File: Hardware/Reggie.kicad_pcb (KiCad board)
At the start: 4 copper layers, 76 parts, among them J1 RBUS, J2 USB_C_Receptacle_USB2.0, U1 ESP32-S3, U2 SN65HVD230, U3 LM66200DRLR, U4 MAX77827AEFD+T, U5 SC4215ASTRT, Y1 R940000171

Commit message: 2nd review of schematic
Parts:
- added C25: 1uF, Capacitor_SMD:C_0402_1005Metric, F.Cu at (86.1, 24.0)
- added C26: 1uF, Capacitor_SMD:C_0402_1005Metric, F.Cu at (86.1, 26.0)
- added C27: 220nF, Capacitor_SMD:C_0402_1005Metric, F.Cu at (86.1, 27.9)
- added C28: 10nF, Capacitor_SMD:C_0402_1005Metric, F.Cu at (86.1, 29.9)
- added C29: 10nF, Capacitor_SMD:C_0402_1005Metric, F.Cu at (86.1, 31.9)
- added C30: 10nF, Capacitor_SMD:C_0402_1005Metric, F.Cu at (86.1, 33.9)
- added C31: 0.01uF, Capacitor_SMD:C_0402_1005Metric, F.Cu at (110.3, 59.0)
- added C32: 0.1uF, Capacitor_SMD:C_0402_1005Metric, F.Cu at (110.3, 61.0)
- added C33: 0.01uF, Capacitor_SMD:C_0402_1005Metric, F.Cu at (110.3, 63.0)
- added C34: 0.1uF, Capacitor_SMD:C_0402_1005Metric, F.Cu at (110.3, 64.9)
- added C35: 0.1uF, Capacitor_SMD:C_0402_1005Metric, F.Cu at (110.3, 66.9)
- added C36: 0.01uF, Capacitor_SMD:C_0402_1005Metric, F.Cu at (113.2, 59.0)
- added C37: 0.1uF, Capacitor_SMD:C_0402_1005Metric, F.Cu at (113.2, 61.0)
- added C38: 0.01uF, Capacitor_SMD:C_0402_1005Metric, F.Cu at (113.2, 63.0)
- added C39: 0.1uF, Capacitor_SMD:C_0402_1005Metric, F.Cu at (113.2, 64.9)
- added C40: 0.1uF, Capacitor_SMD:C_0402_1005Metric, F.Cu at (113.2, 66.9)
- added C41: 2.2uF, Capacitor_SMD:C_0603_1608Metric, F.Cu at (80.6, 58.0)
- added C42: 180pF, Capacitor_SMD:C_0402_1005Metric, F.Cu at (66.9, 63.0)
- added C43: 3.9nF, Capacitor_SMD:C_0402_1005Metric, F.Cu at (66.9, 65.0)
- added C44: 1uF, Capacitor_SMD:C_0402_1005Metric, F.Cu at (66.9, 66.9)
- added C45: 22uF, Capacitor_SMD:C_0805_2012Metric, F.Cu at (76.4, 58.3)
- added C46: 22uF, Capacitor_SMD:C_0805_2012Metric, F.Cu at (76.4, 61.3)
- added C47: 100nF, Capacitor_SMD:C_0402_1005Metric, F.Cu at (66.9, 68.9)
- added C48: 2.2uF, Capacitor_SMD:C_0402_1005Metric, F.Cu at (66.9, 70.9)
- added C49: 100nF, Capacitor_SMD:C_0402_1005Metric, F.Cu at (69.8, 63.0)
- added C50: 47uF, Capacitor_SMD:C_1206_3216Metric, F.Cu at (77.0, 51.7)
- added C51: 10uF, Capacitor_SMD:C_0603_1608Metric, F.Cu at (80.6, 60.5)
- added C52: 100nF, Capacitor_SMD:C_0402_1005Metric, F.Cu at (69.8, 65.0)
- added C53: 1uF, Capacitor_SMD:C_0402_1005Metric, F.Cu at (69.8, 66.9)
- added C54: 10uF, Capacitor_SMD:C_0603_1608Metric, F.Cu at (80.6, 63.0)
- added C55: 120pF, Capacitor_SMD:C_0402_1005Metric, F.Cu at (69.8, 68.9)
- added C56: 2.2nF, Capacitor_SMD:C_0402_1005Metric, F.Cu at (69.8, 70.9)
- added C57: 22uF, Capacitor_SMD:C_0805_2012Metric, F.Cu at (76.4, 64.3)
- added C58: 2.2uF, Capacitor_SMD:C_0402_1005Metric, F.Cu at (72.6, 63.0)
- added C59: 22uF, Capacitor_SMD:C_0805_2012Metric, F.Cu at (76.4, 67.3)
- added C60: 100nF, Capacitor_SMD:C_0402_1005Metric, F.Cu at (72.6, 65.0)
- added C61: 100nF, Capacitor_SMD:C_0402_1005Metric, F.Cu at (72.6, 66.9)
- added C62: 10uF, Capacitor_SMD:C_0603_1608Metric, F.Cu at (80.6, 65.5)
- added C63: 100nF, Capacitor_SMD:C_0402_1005Metric, F.Cu at (72.6, 68.9)
- added C64: 22uF, Capacitor_SMD:C_1206_3216Metric, F.Cu at (77.0, 55.1)
- added C65: 1uF, Capacitor_SMD:C_0402_1005Metric, F.Cu at (102.5, 31.1)
- added C66: 4.7uF, Capacitor_SMD:C_0402_1005Metric, F.Cu at (102.5, 33.1)
- added C67: 100uF, Capacitor_Tantalum_SMD:CP_EIA-7360-38_Kemet-E, F.Cu at (106.0, 12.9)
- added C68: 47uF, Capacitor_SMD:C_1206_3216Metric, F.Cu at (98.2, 10.8)
- added C69: 47uF, Capacitor_SMD:C_1206_3216Metric, F.Cu at (98.2, 14.1)
- added C70: 100nF, Capacitor_SMD:C_0402_1005Metric, F.Cu at (102.5, 35.1)
- added C71: 47uF, Capacitor_SMD:C_1206_3216Metric, F.Cu at (98.2, 17.5)
- added C72: 47uF, Capacitor_SMD:C_1206_3216Metric, F.Cu at (98.2, 20.8)
- added C73: 47uF, Capacitor_SMD:C_1206_3216Metric, F.Cu at (98.2, 24.2)
- added C74: 0.1uF, Capacitor_SMD:C_0402_1005Metric, F.Cu at (102.5, 37.1)
- added C75: 160pF, Capacitor_SMD:C_0603_1608Metric, F.Cu at (105.9, 31.4)
- added C76: 47uF, Capacitor_SMD:C_1206_3216Metric, F.Cu at (98.2, 27.5)
- added C77: 100uF, Capacitor_Tantalum_SMD:CP_EIA-7360-38_Kemet-E, F.Cu at (106.0, 20.4)
- added C78: 47uF, Capacitor_SMD:C_1206_3216Metric, F.Cu at (98.2, 30.9)
- added C79: 47uF, Capacitor_SMD:C_1206_3216Metric, F.Cu at (98.2, 34.2)
- added C80: 47uF, Capacitor_SMD:C_1206_3216Metric, F.Cu at (98.2, 37.6)
- added C81: 47uF, Capacitor_SMD:C_1206_3216Metric, F.Cu at (98.2, 40.9)
- added C82: 0.1uF, Capacitor_SMD:C_0402_1005Metric, F.Cu at (91.0, 55.0)
- added J4: 1053131104, Connector_Molex:Molex_Nano-Fit_105313-xx04_1x04_P2.50mm_Horizontal, F.Cu at (67.6, 11.8)
- added J5: 1053131104, Connector_Molex:Molex_Nano-Fit_105313-xx04_1x04_P2.50mm_Horizontal, F.Cu at (67.6, 24.8)
- added J6: 1053131104, Connector_Molex:Molex_Nano-Fit_105313-xx04_1x04_P2.50mm_Horizontal, F.Cu at (67.6, 37.8)
- added JP10: SolderJumper_3_Open, Jumper:SolderJumper-3_P1.3mm_Open_RoundedPad1.0x1.5mm_NumberLabels, F.Cu at (81.8, 25.1)
- added JP11: SolderJumper_3_Open, Jumper:SolderJumper-3_P1.3mm_Open_RoundedPad1.0x1.5mm_NumberLabels, F.Cu at (81.8, 28.6)
- added JP12: SolderJumper_3_Open, Jumper:SolderJumper-3_P1.3mm_Open_RoundedPad1.0x1.5mm_NumberLabels, F.Cu at (81.8, 32.2)
- added JP13: SolderJumper_3_Open, Jumper:SolderJumper-3_P1.3mm_Open_RoundedPad1.0x1.5mm_NumberLabels, F.Cu at (81.8, 35.7)
- added JP15: SolderJumper_3_Open, Jumper:SolderJumper-3_P1.3mm_Open_RoundedPad1.0x1.5mm_NumberLabels, F.Cu at (81.8, 39.3)
- added JP4: SolderJumper_3_Open, Jumper:SolderJumper-3_P1.3mm_Open_RoundedPad1.0x1.5mm_NumberLabels, F.Cu at (81.8, 10.9)
- added JP5: SolderJumper_3_Open, Jumper:SolderJumper-3_P1.3mm_Open_RoundedPad1.0x1.5mm_NumberLabels, F.Cu at (81.8, 14.4)
- added JP6: SolderJumper_3_Open, Jumper:SolderJumper-3_P1.3mm_Open_RoundedPad1.0x1.5mm_NumberLabels, F.Cu at (81.8, 18.0)
- added JP7: SolderJumper_3_Open, Jumper:SolderJumper-3_P1.3mm_Open_RoundedPad1.0x1.5mm_NumberLabels, F.Cu at (81.8, 21.5)
- added Q2: PMOS, Package_TO_SOT_SMD:SOT-23, F.Cu at (87.1, 52.3)
- added R21: 75k, Resistor_SMD:R_0402_1005Metric, F.Cu at (86.1, 10.1)
- added R22: 14k, Resistor_SMD:R_0402_1005Metric, F.Cu at (86.1, 12.1)
- added R23: 10k, Resistor_SMD:R_0402_1005Metric, F.Cu at (86.1, 14.1)
- added R24: 75k, Resistor_SMD:R_0402_1005Metric, F.Cu at (86.1, 16.1)
- added R25: 14k, Resistor_SMD:R_0402_1005Metric, F.Cu at (86.1, 18.1)
- added R26: 10k, Resistor_SMD:R_0402_1005Metric, F.Cu at (86.1, 20.0)
- added R27: 1k, Resistor_SMD:R_0402_1005Metric, F.Cu at (86.1, 22.0)
- added R28: 1k, Resistor_SMD:R_0402_1005Metric, F.Cu at (89.0, 10.1)
- added R29: 49.9, Resistor_SMD:R_0402_1005Metric, F.Cu at (89.0, 12.1)
- added R30: 49.9, Resistor_SMD:R_0402_1005Metric, F.Cu at (89.0, 14.1)
- added R31: 1k, Resistor_SMD:R_0402_1005Metric, F.Cu at (89.0, 16.1)
- added R32: 1k, Resistor_SMD:R_0402_1005Metric, F.Cu at (89.0, 18.1)
- added R33: 75k, Resistor_SMD:R_0402_1005Metric, F.Cu at (89.0, 20.0)
- added R34: 14k, Resistor_SMD:R_0402_1005Metric, F.Cu at (89.0, 22.0)
- added R35: 10k, Resistor_SMD:R_0402_1005Metric, F.Cu at (91.9, 10.1)
- added R36: 1k, Resistor_SMD:R_0402_1005Metric, F.Cu at (91.9, 12.1)
- added R37: 49.9, Resistor_SMD:R_0402_1005Metric, F.Cu at (91.9, 14.1)
- added R38: 1k, Resistor_SMD:R_0402_1005Metric, F.Cu at (91.9, 16.1)
- added R39: 100, Resistor_SMD:R_0402_1005Metric, F.Cu at (116.1, 59.0)
- added R40: 100, Resistor_SMD:R_0402_1005Metric, F.Cu at (116.1, 61.0)
- added R41: 100, Resistor_SMD:R_0402_1005Metric, F.Cu at (116.1, 63.0)
- added R42: 100, Resistor_SMD:R_0402_1005Metric, F.Cu at (116.1, 65.0)
- added R43: 7.87k, Resistor_SMD:R_0402_1005Metric, F.Cu at (66.9, 51.1)
- added R44: 360k, Resistor_SMD:R_0402_1005Metric, F.Cu at (66.9, 53.0)
- added R45: 100k, Resistor_SMD:R_0402_1005Metric, F.Cu at (66.9, 55.0)
- added R46: 10K, Resistor_SMD:R_0402_1005Metric, F.Cu at (66.9, 57.0)
- added R47: 560k, Resistor_SMD:R_0402_1005Metric, F.Cu at (66.9, 59.0)
- added R48: 49.9k, Resistor_SMD:R_0402_1005Metric, F.Cu at (66.9, 61.0)
- added R49: 150k, Resistor_SMD:R_0603_1608Metric, F.Cu at (80.6, 68.1)
- added R50: 301k, Resistor_SMD:R_0402_1005Metric, F.Cu at (69.8, 51.1)
- added R51: 18.7k, Resistor_SMD:R_0402_1005Metric, F.Cu at (69.8, 53.0)
- added R52: 976k, Resistor_SMD:R_0402_1005Metric, F.Cu at (69.8, 55.0)
- added R53: 100k, Resistor_SMD:R_0402_1005Metric, F.Cu at (69.8, 57.0)
- added R54: 49.9k, Resistor_SMD:R_0402_1005Metric, F.Cu at (69.8, 59.0)
- added R55: 432k, Resistor_SMD:R_0402_1005Metric, F.Cu at (69.8, 61.0)
- added R56: 10K, Resistor_SMD:R_0402_1005Metric, F.Cu at (72.7, 51.1)
- added R57: 475k, Resistor_SMD:R_0402_1005Metric, F.Cu at (72.7, 53.0)
- added R58: 287k, Resistor_SMD:R_0402_1005Metric, F.Cu at (72.7, 55.0)
- added R59: 10k, Resistor_SMD:R_0402_1005Metric, F.Cu at (102.5, 25.2)
- added R60: 113k, Resistor_SMD:R_0402_1005Metric, F.Cu at (102.5, 27.2)
- added R61: 10k, Resistor_SMD:R_0402_1005Metric, F.Cu at (102.5, 29.2)
- added R62: 2.2, Resistor_SMD:R_0402_1005Metric, F.Cu at (105.4, 25.2)
- added R63: 1k, Resistor_SMD:R_0402_1005Metric, F.Cu at (105.4, 27.2)
- added R64: 442k, Resistor_SMD:R_0402_1005Metric, F.Cu at (105.4, 29.2)
- added R65: 200k, Resistor_SMD:R_0402_1005Metric, F.Cu at (108.3, 25.2)
- added R66: 100k, Resistor_SMD:R_0402_1005Metric, F.Cu at (108.3, 27.2)
- added R67: 10k, Resistor_SMD:R_0402_1005Metric, F.Cu at (108.3, 29.2)
- added R68: 5.1R, Resistor_SMD:R_0603_1608Metric, F.Cu at (105.9, 33.9)
- added R69: 1k, Resistor_SMD:R_0402_1005Metric, F.Cu at (91.0, 51.1)
- added R70: 10k, Resistor_SMD:R_0402_1005Metric, F.Cu at (91.0, 53.0)
- added TC1: Thermocouple, Connector_Molex:Molex_Nano-Fit_105313-xx02_1x02_P2.50mm_Horizontal, F.Cu at (97.5, 47.3)
- added TC2: Thermocouple, Connector_Molex:Molex_Nano-Fit_105313-xx02_1x02_P2.50mm_Horizontal, F.Cu at (97.5, 55.3)
- added U6: MAX31856, Package_SO:TSSOP-14_4.4x5mm_P0.65mm, F.Cu at (113.3, 48.0)
- added U7: MAX31856, Package_SO:TSSOP-14_4.4x5mm_P0.65mm, F.Cu at (113.3, 54.8)
- renumbered C13 to C12, C14 to C13, C15 to C14, C16 to C15, C17 to C16, C20 to C17, C21 to C18, C22 to C19, C23 to C20, C24 to C21, C25 to C22, C26 to C23, C27 to C24, JP2 to JP1, JP3 to JP2, JP1 to JP3, R8 to R10, R9 to R11, R10 to R12, R11 to R13, R12 to R14, R13 to R15, R14 to R16, R15 to R17, R16 to R18, R17 to R19, R5 to R3, R18 to R4, R3 to R5, R4 to R6, R6 to R7, R7 to R8, TP9 to TP1, TP10 to TP2, TP1 to TP3, TP2 to TP4, TP4 to TP5, TP5 to TP6, TP6 to TP7
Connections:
- U1 pad 10: unconnected-(U1-GPIO5/ADC1_CH4-Pad10) -> /ADS_DRDY
- U1 pad 11: unconnected-(U1-GPIO6/ADC1_CH5-Pad11) -> /ADS_CLK
- U1 pad 12: unconnected-(U1-GPIO7/ADC1_CH6-Pad12) -> /T_FAULT0
- U1 pad 13: unconnected-(U1-GPIO8/ADC1_CH7-Pad13) -> /T_DRDY0
- U1 pad 23: unconnected-(U1-GPIO17/ADC2_CH6/DAC_2-Pad23) -> /ADS_CS
- U1 pad 27: unconnected-(U1-GPIO21-Pad27) -> /T_CS0
- U1 pad 36: unconnected-(U1-SPICLK_N/GPIO48-Pad36) -> /BuckPGOOD
- U1 pad 37: unconnected-(U1-SPICLK_P/GPIO47-Pad37) -> /BUCK_EN
- U1 pad 38: unconnected-(U1-GPIO33-Pad38) -> /ServoPWM
- U1 pad 39: unconnected-(U1-GPIO34-Pad39) -> /VSPI_MOSI
- U1 pad 40: unconnected-(U1-GPIO35-Pad40) -> /VSPI_MISO
- U1 pad 41: unconnected-(U1-GPIO36-Pad41) -> /VSPI_SCLK
- U1 pad 42: unconnected-(U1-GPIO37-Pad42) -> /SD1_CS
- U1 pad 43: unconnected-(U1-GPIO38-Pad43) -> /SD_DET
- U1 pad 45: unconnected-(U1-MTDO/JTAG/GPIO40-Pad45) -> /T_CS1
- U1 pad 47: unconnected-(U1-MTDI/JTAG/GPIO41-Pad47) -> /T_FAULT1
- U1 pad 48: unconnected-(U1-MTMS/JTAG/GPIO42-Pad48) -> /T_DRDY1
- U1 pad 51: unconnected-(U1-GPIO45-Pad51) -> /SD_EN

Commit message: pcb update
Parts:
- added IC2: TPS61089RNRR, iclr:IC_TPS61089RNRR, F.Cu at (240.9, 99.3)
- added IC3: AP2205-W5-7, iclr:SOT95P282X145-5N, F.Cu at (258.2, 98.8)
- added IC4: AP2205-W5-7, iclr:SOT95P282X145-5N, F.Cu at (258.7, 115.4)
- added IC5: TPS61089RNRR, iclr:IC_TPS61089RNRR, F.Cu at (241.8, 126.3)
- added J7: ST1W008S4TR2000, iclr:JAE_ST1W008S4TR2000, F.Cu at (172.9, 79.1)
- added JP14: SolderJumper_2_Open, iclr:SmallerSolderJP, F.Cu at (240.0, 21.0)
- added JP16: SolderJumper_2_Open, iclr:SmallerSolderJP, F.Cu at (158.9, 81.0)
- added JP8: SolderJumper_2_Open, iclr:SmallerSolderJP, F.Cu at (240.0, 15.9)
- added JP9: SolderJumper_2_Open, iclr:SmallerSolderJP, F.Cu at (240.0, 18.4)
- added L4: SRR6038-5R0Y, iclr:IND_SRP6540-390M, F.Cu at (243.2, 92.8)
- added L5: SRR6038-5R0Y, iclr:IND_SRP6540-390M, F.Cu at (242.2, 119.8)
- added L6: 3.3uH, iclr:IND_SPM10065VT-3R3M-D, F.Cu at (152.4, 141.1)
- added Q1: SSM3K15AMFV,L3F, iclr:SOT-723, F.Cu at (121.4, 154.6)
- added R20: 165, Resistor_SMD:R_0402_1005Metric, F.Cu at (172.0, 59.8)
- added R9: R, Resistor_SMD:R_0402_1005Metric, F.Cu at (172.9, 62.8)
- added U8: SiC437AED-T1, iclr:SiC437BEDT1GE3, F.Cu at (134.6, 142.3)
- moved J1 212.6 mm to (147.8, 176.6)
- moved R54 201.5 mm to (263.2, 115.8), turned to 180 degrees
- moved J4 201.3 mm to (262.5, 62.3)
- moved R48 200.2 mm to (263.4, 99.5), turned to 180 degrees
- moved R55 199.2 mm to (261.4, 115.3), turned to 90 degrees
- moved C48 198.4 mm to (263.4, 98.0)
- moved C58 197.4 mm to (263.2, 114.6)
- moved C77 194.1 mm to (21.4, 195.1)
- moved C25 192.5 mm to (278.5, 29.8)
- moved C26 192.5 mm to (278.5, 31.7)
- moved C27 192.5 mm to (278.5, 33.7)
- moved C29 192.5 mm to (278.5, 37.6)
- moved C30 192.5 mm to (278.5, 39.6)
- moved J5 192.5 mm to (260.0, 30.6)
- moved J6 192.5 mm to (260.0, 43.6)
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
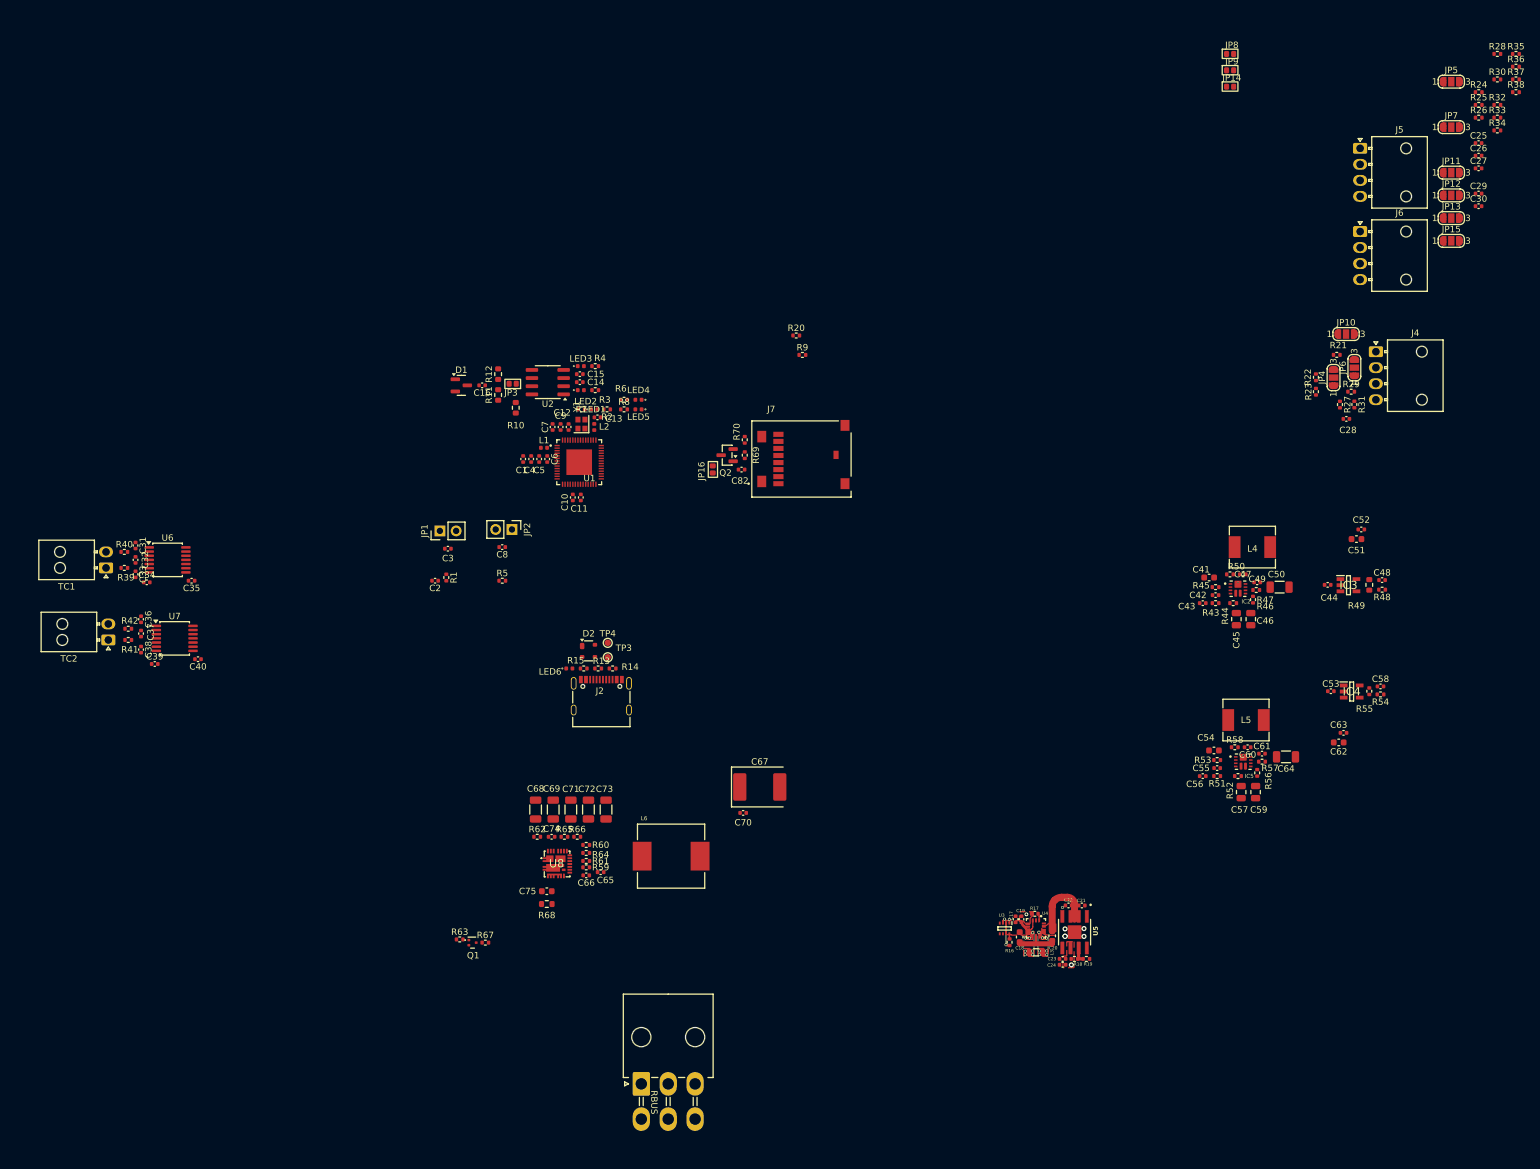
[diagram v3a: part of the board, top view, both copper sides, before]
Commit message: pcb and schematic update
Found all footprints including J3, pressure controller, tvs diode. PCB infrastructure update
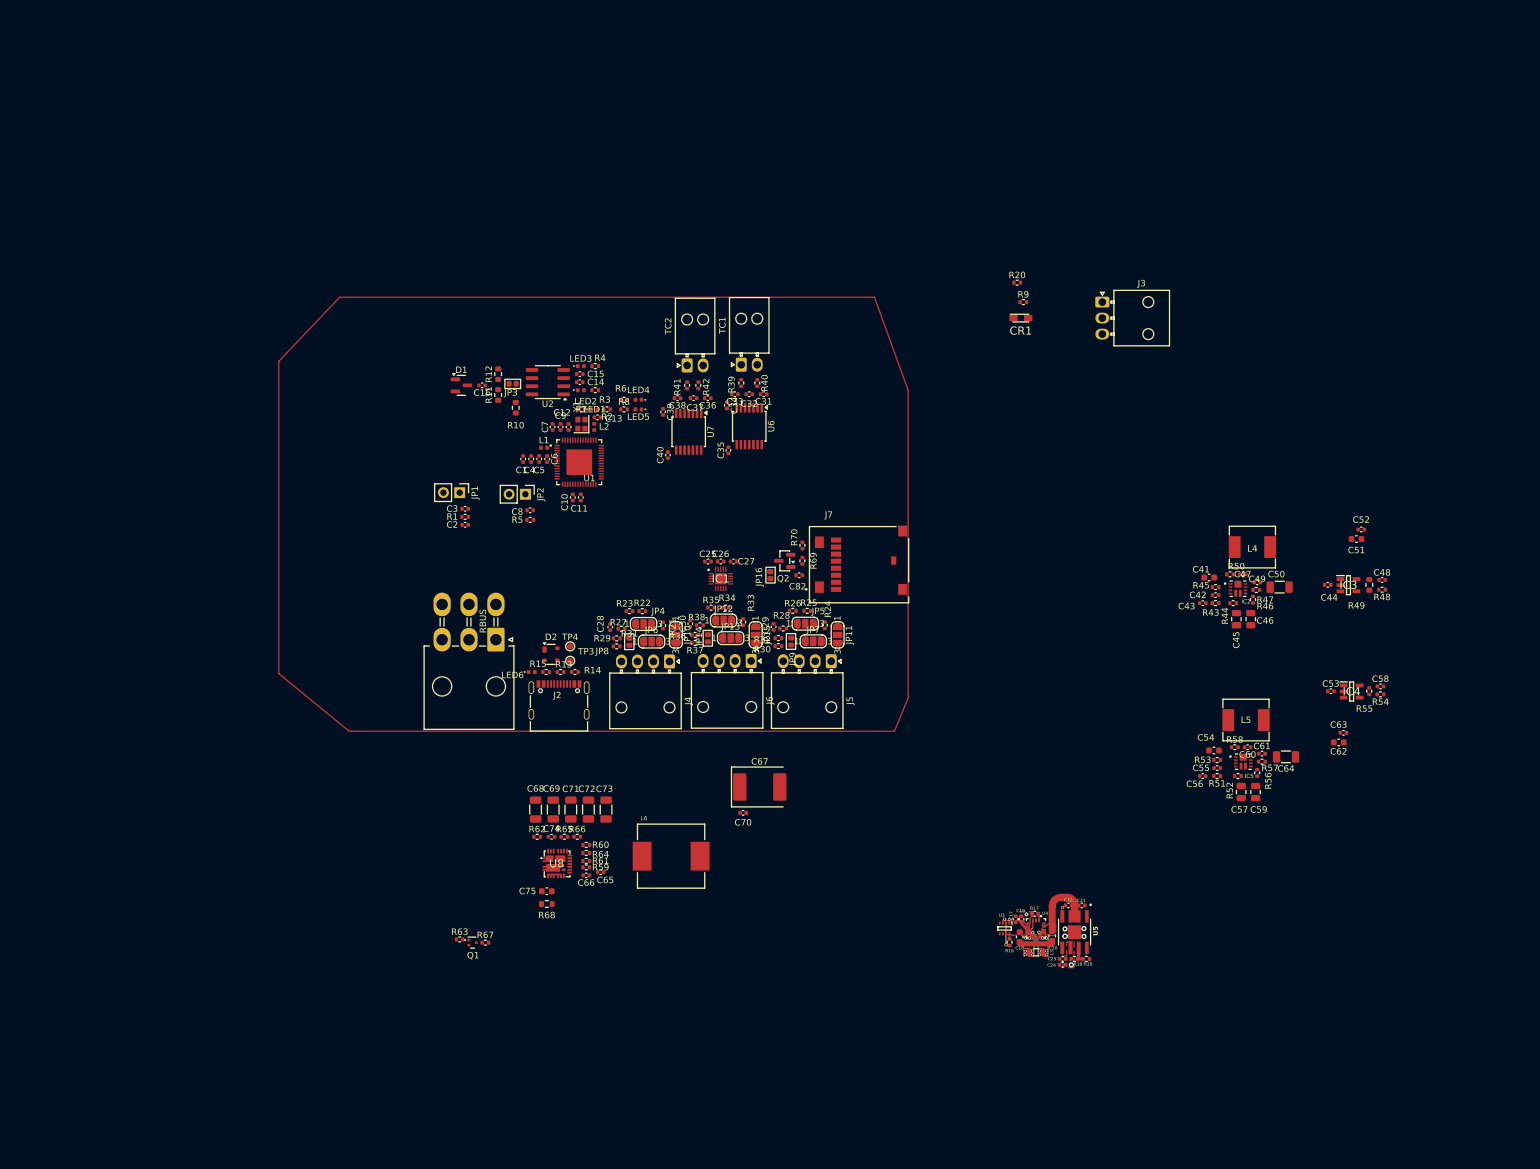
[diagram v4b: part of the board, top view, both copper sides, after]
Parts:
- added CR1: CPDF3V3UP-HF, Diode_SMD:DIOM2512X90N, F.Cu at (207.0, 57.1)
- added IC1: ADS131M04IRUKR, iclr:QFN40P300X300X80-21N-D, F.Cu at (160.2, 97.8)
- added J3: ServoConnector1, Connector_Molex:Molex_Nano-Fit_105313-xx03_1x03_P2.50mm_Horizontal, F.Cu at (219.7, 54.6)
- moved R36 155.9 mm to (156.2, 106.5), turned to 180 degrees
- moved R37 155.4 mm to (156.2, 107.8), turned to 180 degrees
- moved R35 152.5 mm to (158.7, 102.3)
- moved R38 152.2 mm to (156.9, 105.0), turned to 180 degrees
- moved R28 143.1 mm to (169.9, 105.5), turned to 180 degrees
- moved R30 142.9 mm to (169.2, 108.3), turned to 180 degrees
- moved R34 141.7 mm to (160.9, 102.3), turned to 180 degrees
- moved R33 141.6 mm to (163.7, 104.5), turned to 90 degrees
- moved R32 139.7 mm to (169.2, 107.0), turned to 180 degrees
- moved C30 139.3 mm to (155.4, 104.8), turned to 90 degrees
- moved C25 136.9 mm to (158.2, 95.1)
- moved C26 134.2 mm to (160.2, 95.1)
- moved R26 131.9 mm to (171.4, 102.8)
- moved R24 131.7 mm to (176.4, 105.0), turned to 90 degrees
- moved JP5 131.6 mm to (173.4, 104.8)
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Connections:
- C82 pad 1: Net-(JP16-B) -> +3V3
- J7 pad C4: Net-(JP16-B) -> +3V3
- R69 pad 2: /SD_EN -> +3V3
- U1 pad 51: /SD_EN -> +3V3

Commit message: PCB update
packing update
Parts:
- moved TP2 125.9 mm to (143.7, 75.1)
- moved TP1 125.4 mm to (145.7, 65.1)
- moved C17 94.8 mm to (132.5, 91.3)
- moved C18 94.8 mm to (133.1, 94.1)
- moved C19 94.8 mm to (133.4, 91.3)
- moved C24 94.8 mm to (139.8, 98.4)
- moved L3 94.8 mm to (135.6, 96.5)
- moved R16 94.8 mm to (131.5, 94.9)
- moved R17 94.8 mm to (135.5, 90.5)
- moved R18 94.8 mm to (141.6, 97.5)
- moved R19 94.8 mm to (143.5, 97.5)
- moved U3 94.8 mm to (130.7, 92.8)
- moved U4 94.8 mm to (135.6, 92.7)
- moved U5 94.8 mm to (141.7, 93.3)
- moved C20 94.8 mm to (138.2, 93.9)
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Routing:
- net Net-(JP8-A): track 0.00 -> 1.56 mm
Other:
- board outline added: 79.5 x 65.8 mm
